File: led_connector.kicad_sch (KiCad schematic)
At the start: 7 parts, among them J3 SM02B-SRSS-TB-LF-SN, J4 SM02B-SRSS-TB-LF-SN

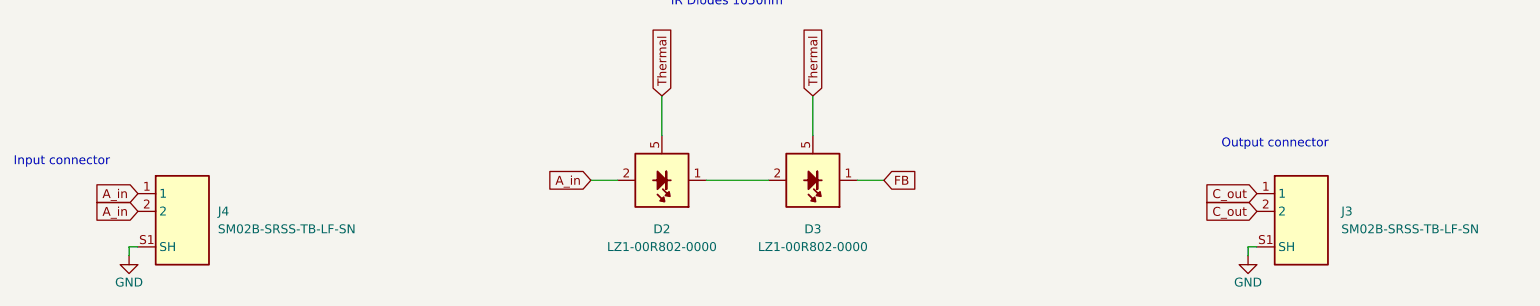
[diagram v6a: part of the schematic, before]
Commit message: [50954] Added CC resistors and OHP assets, updated README
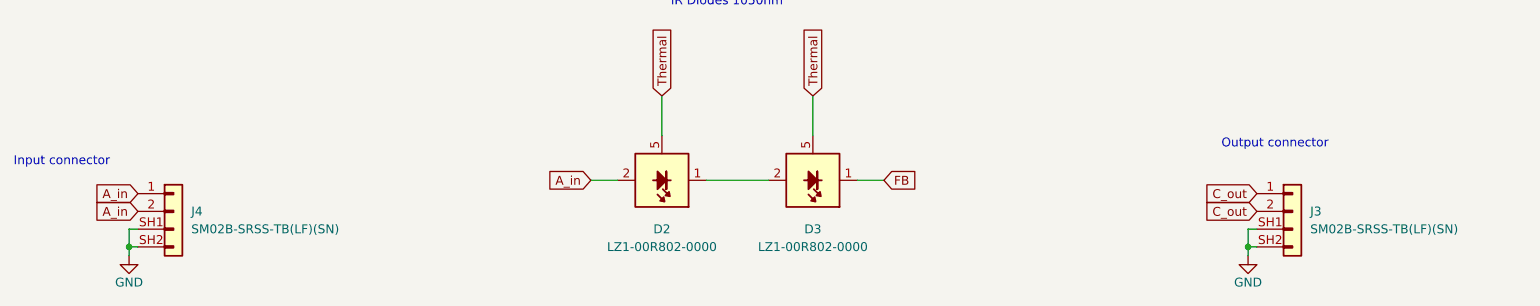
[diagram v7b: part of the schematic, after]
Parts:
- removed J3, J4: SM02B-SRSS-TB-LF-SN, antmicro-footprints:JST_SM02B-SRSS-TB-LF-SN, symbol antmicroRectangularConnectorsHeadersMalePins:SM02B-SRSS-TB-LF-SN
- added J3, J4: JST_SH_1x2_SM02B-SRSS-TB-LF-SN, antmicro-footprints:Conn_JST_SH_1x2_SM02B-SRSS-TB-LF-SN, symbol antmicroWire2BoardConnectors:JST_SH_1x2_SM02B-SRSS-TB-LF-SN
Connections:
- net A_in: now also J4.1, J4.2
- net C_out: now also J3.1, J3.2
- net GND: now also J3.SH1, J3.SH2, J4.SH1, J4.SH2
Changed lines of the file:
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@@
   (title_block
     (title "LZ1 OSRAM LuxiGen LED Driver")
-    (date "2023-07-20")
+    (date "2023-11-03")
     (rev "1.1.1")
     (company "Antmicro Ltd.")
     (comment 1 "www.antmicro.com")
   )
+  (junction (at 62.23 109.22) (diameter 0) (color 0 0 0 0)
+  )
   (junction (at 144.145 39.37) (diameter 0) (color 0 0 0 0)
   )
   (junction (at 156.21 52.705) (diameter 0) (color 0 0 0 0)
   )
+  (junction (at 222.25 109.22) (diameter 0) (color 0 0 0 0)
+  )
   (polyline (pts (xy 133.35 17.78) (xy 133.35 31.115))
     (stroke (width 0) (type default) (color 0 0 0 0))
@@
     (stroke (width 0) (type default) (color 0 0 0 0))
   )
+  (wire (pts (xy 222.25 106.68) (xy 222.25 109.22))
+    (stroke (width 0) (type default) (color 0 0 0 0))
+  )
   (wire (pts (xy 222.25 110.49) (xy 222.25 109.22))
     (stroke (width 0) (type default) (color 0 0 0 0))
@@
     (stroke (width 0) (type default) (color 0 0 0 0))
   )
+  (wire (pts (xy 62.23 106.68) (xy 62.23 109.22))
+    (stroke (width 0) (type default) (color 0 0 0 0))
+  )
   (polyline (pts (xy 163.195 17.78) (xy 163.195 31.115))
     (stroke (width 0) (type default) (color 0 0 0 0))
@@
     (stroke (width 0) (type default) (color 0 0 0 0))
   )
+  (wire (pts (xy 223.52 106.68) (xy 222.25 106.68))
+    (stroke (width 0) (type default) (color 0 0 0 0))
+  )
   (wire (pts (xy 144.145 39.37) (xy 144.145 45.085))
     (stroke (width 0) (type default) (color 0 0 0 0))
@@
   )
   (wire (pts (xy 138.43 93.345) (xy 138.43 87.63))
+    (stroke (width 0) (type default) (color 0 0 0 0))
+  )
+  (wire (pts (xy 63.5 106.68) (xy 62.23 106.68))
     (stroke (width 0) (type default) (color 0 0 0 0))
   )
@@
     (pin "5")
   )
+  (symbol (lib_id "antmicroWire2BoardConnectors:JST_SH_1x2_SM02B-SRSS-TB-LF-SN") (at 63.5 101.6 0) (unit 1)
+    (in_bom yes) (on_board yes) (fields_autoplaced)
+    (property "Reference" "J4" (id 0) (at 71.12 104.1399 0)
+      (effects (font (size 1.27 1.27) (thickness 0.15)) (justify left))
+    )
+    (property "Value" "JST_SH_1x2_SM02B-SRSS-TB-LF-SN" (id 1) (at 90.17 107.95 0)
+      (effects (font (size 1.27 1.27) (thickness 0.15)) (justify left bottom) hide)
+    )
+    (property "Footprint" "antmicro-footprints:Conn_JST_SH_1x2_SM02B-SRSS-TB-LF-SN" (id 2) (at 90.17 110.49 0)
+      (effects (font (size 1.27 1.27) (thickness 0.15)) (justify left bottom) hide)
+    )
+    (property "Datasheet" "https://www.jst-mfg.com/product/pdf/eng/eSH.pdf" (id 3) (at 90.17 113.03 0)
+      (effects (font (size 1.27 1.27) (thickness 0.15)) (justify left bottom) hide)
+    )
+    (property "MPN" "SM02B-SRSS-TB(LF)(SN)" (id 4) (at 71.12 106.6799 0)
+      (effects (font (size 1.27 1.27) (thickness 0.15)) (justify left))
+    )
+    (property "Manufacturer" "JST Automotive Connectors" (id 5) (at 90.17 118.11 0)
+      (effects (font (size 1.27 1.27) (thickness 0.15)) (justify left bottom) hide)
+    )
+    (property "Author" "Antmicro" (id 6) (at 90.17 120.65 0)
+      (effects (font (size 1.27 1.27) (thickness 0.15)) (justify left bottom) hide)
+    )
+    (property "License" "Apache-2.0" (id 7) (at 90.17 123.19 0)
+      (effects (font (size 1.27 1.27) (thickness 0.15)) (justify left bottom) hide)
+    )
+    (pin "1")
+    (pin "2")
+    (pin "SH1")
+    (pin "SH2")
+  )
   (symbol (lib_id "antmicropower:GND") (at 62.23 110.49 0) (unit 1)
     (in_bom yes) (on_board yes)
@@
     )
     (pin "1")
-  )
-  (symbol (lib_id "antmicroRectangularConnectorsHeadersMalePins:SM02B-SRSS-TB-LF-SN") (at 223.52 101.6 0) (unit 1)
-    (in_bom yes) (on_board yes) (fields_autoplaced)
-    (property "Reference" "J3" (id 0) (at 235.585 104.1399 0)
-      (effects (font (size 1.27 1.27)) (justify left))
-    )
-    (property "Value" "SM02B-SRSS-TB-LF-SN" (id 1) (at 235.585 106.6799 0)
-      (effects (font (size 1.27 1.27)) (justify left))
-    )
-    (property "Footprint" "antmicro-footprints:JST_SM02B-SRSS-TB-LF-SN" (id 2) (at 250.19 110.49 0)
-      (effects (font (size 1.27 1.27) (thickness 0.15)) (justify left bottom) hide)
-    )
-    (property "Datasheet" "https://www.jst-mfg.com/product/pdf/eng/eSH.pdf" (id 3) (at 250.19 113.03 0)
-      (effects (font (size 1.27 1.27) (thickness 0.15)) (justify left bottom) hide)
-    )
-    (property "MPN" "SM02B-SRSS-TB(LF)(SN)" (id 4) (at 250.19 115.57 0)
-      (effects (font (size 1.27 1.27) (thickness 0.15)) (justify left bottom) hide)
-    )
-    (property "Manufacturer" "JST" (id 5) (at 250.19 118.11 0)
-      (effects (font (size 1.27 1.27) (thickness 0.15)) (justify left bottom) hide)
-    )
-    (property "License" "Apache-2.0" (id 7) (at 250.19 123.19 0)
-      (effects (font (size 1.27 1.27) (thickness 0.15)) (justify left bottom) hide)
-    )
-    (property "Author" "Antmicro" (id 8) (at 250.19 120.65 0)
-      (effects (font (size 1.27 1.27) (thickness 0.15)) (justify left bottom) hide)
-    )
-    (pin "1")
-    (pin "2")
-    (pin "S1")
-    (pin "S2")
   )
   (symbol (lib_id "antmicroLEDIndicationDiscrete:LED_IR_LZ1-00R802") (at 144.78 99.695 180) (unit 1)
@@
     (pin "2")
   )
+  (symbol (lib_id "antmicroWire2BoardConnectors:JST_SH_1x2_SM02B-SRSS-TB-LF-SN") (at 223.52 101.6 0) (unit 1)
+    (in_bom yes) (on_board yes) (fields_autoplaced)
+    (property "Reference" "J3" (id 0) (at 231.14 104.1399 0)
+      (effects (font (size 1.27 1.27) (thickness 0.15)) (justify left))
+    )
+    (property "Value" "JST_SH_1x2_SM02B-SRSS-TB-LF-SN" (id 1) (at 250.19 107.95 0)
+      (effects (font (size 1.27 1.27) (thickness 0.15)) (justify left bottom) hide)
+    )
+    (property "Footprint" "antmicro-footprints:Conn_JST_SH_1x2_SM02B-SRSS-TB-LF-SN" (id 2) (at 250.19 110.49 0)
+      (effects (font (size 1.27 1.27) (thickness 0.15)) (justify left bottom) hide)
+    )
+    (property "Datasheet" "https://www.jst-mfg.com/product/pdf/eng/eSH.pdf" (id 3) (at 250.19 113.03 0)
+      (effects (font (size 1.27 1.27) (thickness 0.15)) (justify left bottom) hide)
+    )
+    (property "MPN" "SM02B-SRSS-TB(LF)(SN)" (id 4) (at 231.14 106.6799 0)
+      (effects (font (size 1.27 1.27) (thickness 0.15)) (justify left))
+    )
+    (property "Manufacturer" "JST Automotive Connectors" (id 5) (at 250.19 118.11 0)
+      (effects (font (size 1.27 1.27) (thickness 0.15)) (justify left bottom) hide)
+    )
+    (property "Author" "Antmicro" (id 6) (at 250.19 120.65 0)
+      (effects (font (size 1.27 1.27) (thickness 0.15)) (justify left bottom) hide)
+    )
+    (property "License" "Apache-2.0" (id 7) (at 250.19 123.19 0)
+      (effects (font (size 1.27 1.27) (thickness 0.15)) (justify left bottom) hide)
+    )
+    (pin "1")
+    (pin "2")
+    (pin "SH1")
+    (pin "SH2")
+  )
   (symbol (lib_name "R_0R_1206_1") (lib_id "antmicroResistorsmisc:R_0R_1206") (at 153.67 39.37 180) (unit 1)
     (in_bom yes) (on_board yes)
@@
     (pin "2")
   )
-  (symbol (lib_name "SM02B-SRSS-TB-LF-SN_1") (lib_id "antmicroRectangularConnectorsHeadersMalePins:SM02B-SRSS-TB-LF-SN") (at 63.5 101.6 0) (unit 1)
-    (in_bom yes) (on_board yes) (fields_autoplaced)
-    (property "Reference" "J4" (id 0) (at 74.93 104.1399 0)
-      (effects (font (size 1.27 1.27)) (justify left))
-    )
-    (property "Value" "SM02B-SRSS-TB-LF-SN" (id 1) (at 74.93 106.6799 0)
-      (effects (font (size 1.27 1.27)) (justify left))
-    )
-    (property "Footprint" "antmicro-footprints:JST_SM02B-SRSS-TB-LF-SN" (id 2) (at 90.17 110.49 0)
-      (effects (font (size 1.27 1.27) (thickness 0.15)) (justify left bottom) hide)
-    )
-    (property "Datasheet" "https://www.jst-mfg.com/product/pdf/eng/eSH.pdf" (id 3) (at 90.17 113.03 0)
-      (effects (font (size 1.27 1.27) (thickness 0.15)) (justify left bottom) hide)
-    )
-    (property "MPN" "SM02B-SRSS-TB(LF)(SN)" (id 4) (at 90.17 115.57 0)
-      (effects (font (size 1.27 1.27) (thickness 0.15)) (justify left bottom) hide)
-    )
-    (property "Manufacturer" "JST" (id 5) (at 90.17 118.11 0)
-      (effects (font (size 1.27 1.27) (thickness 0.15)) (justify left bottom) hide)
-    )
-    (property "License" "Apache-2.0" (id 7) (at 90.17 123.19 0)
-      (effects (font (size 1.27 1.27) (thickness 0.15)) (justify left bottom) hide)
-    )
-    (property "Author" "Antmicro" (id 8) (at 90.17 120.65 0)
-      (effects (font (size 1.27 1.27) (thickness 0.15)) (justify left bottom) hide)
-    )
-    (pin "1")
-    (pin "2")
-    (pin "S1")
-    (pin "S2")
-  )
 )
